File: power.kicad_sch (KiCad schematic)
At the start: 32 parts, among them Q3 AO3400A, U7 SIC431AED-T1-GE3, U9 TPS564247DRLR

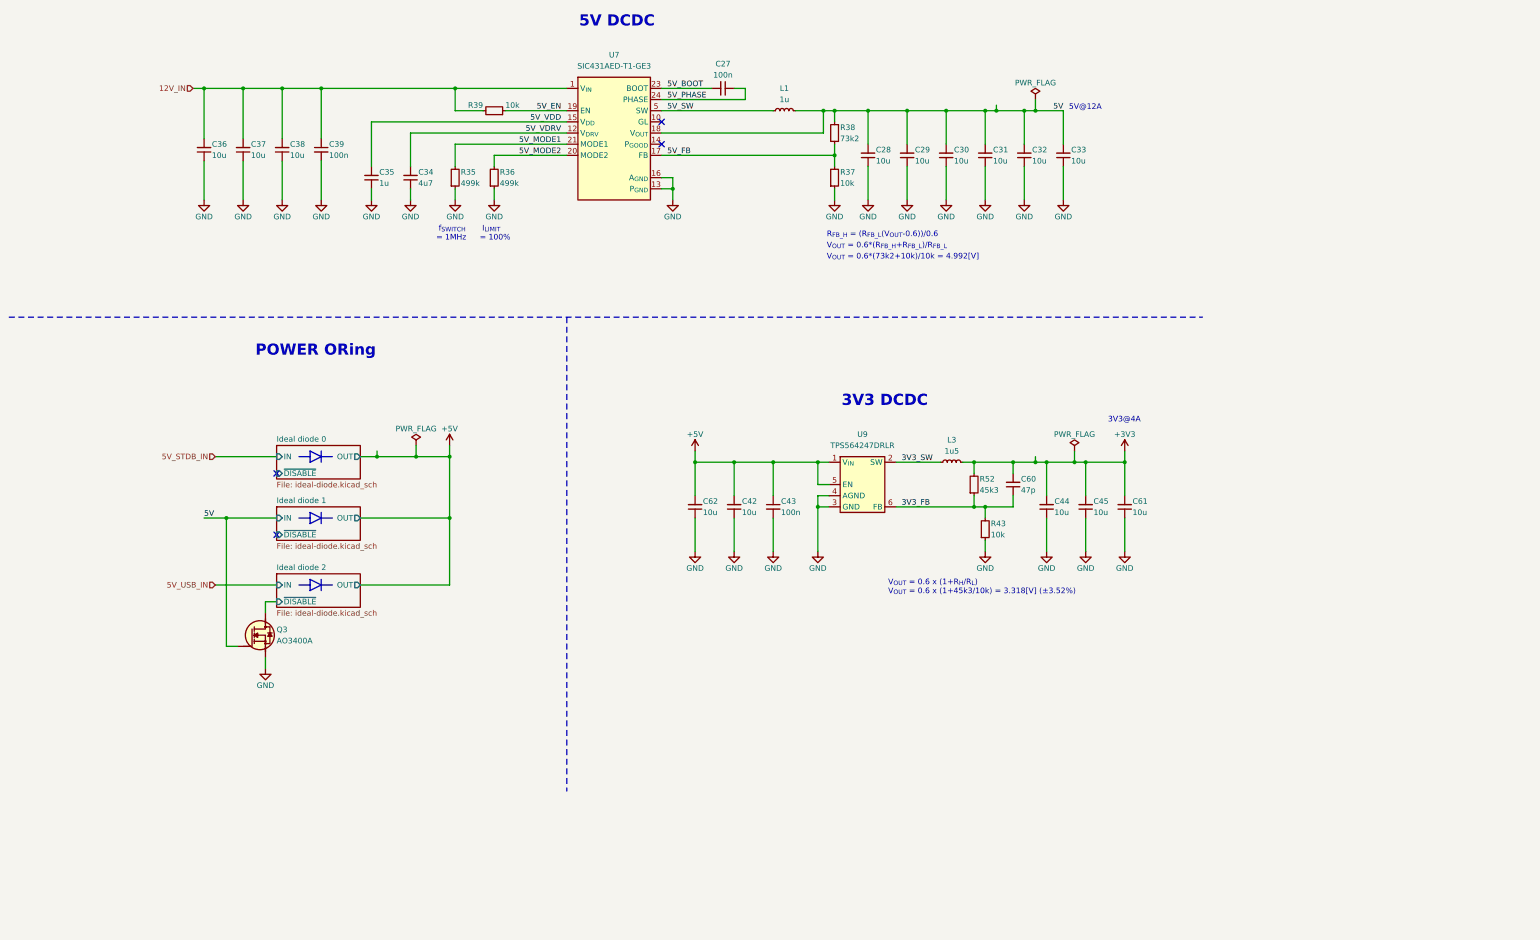
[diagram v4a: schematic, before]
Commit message: [#3] WIP: Clear ERC, re-annotate schematic
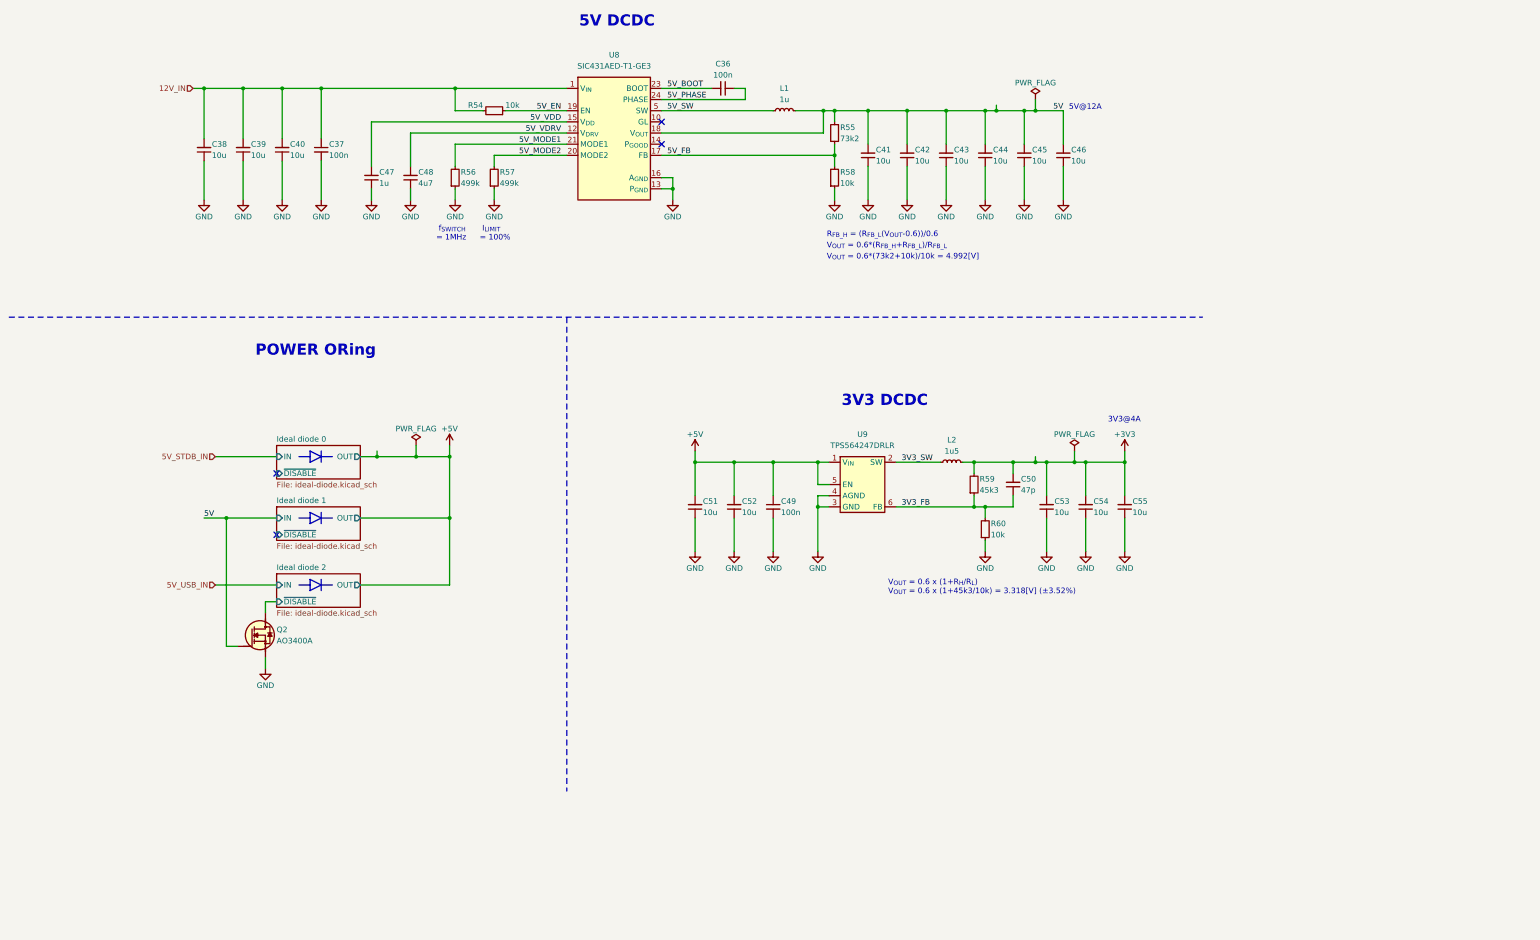
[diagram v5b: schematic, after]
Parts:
- renumbered C27 to C36, C39 to C37, C36 to C38, C37 to C39, C38 to C40, C28 to C41, C29 to C42, C30 to C43, C31 to C44, C32 to C45, C33 to C46, C35 to C47, C34 to C48, C43 to C49, C60 to C50, C62 to C51, C42 to C52, C44 to C53, C45 to C54, C61 to C55, L3 to L2, Q3 to Q2, R39 to R54, R38 to R55, R35 to R56, R36 to R57, R37 to R58, R52 to R59, R43 to R60, U7 to U8

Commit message: [#3] Add 0R to DC-DC outputs, add 5V->3V3 power sequencing
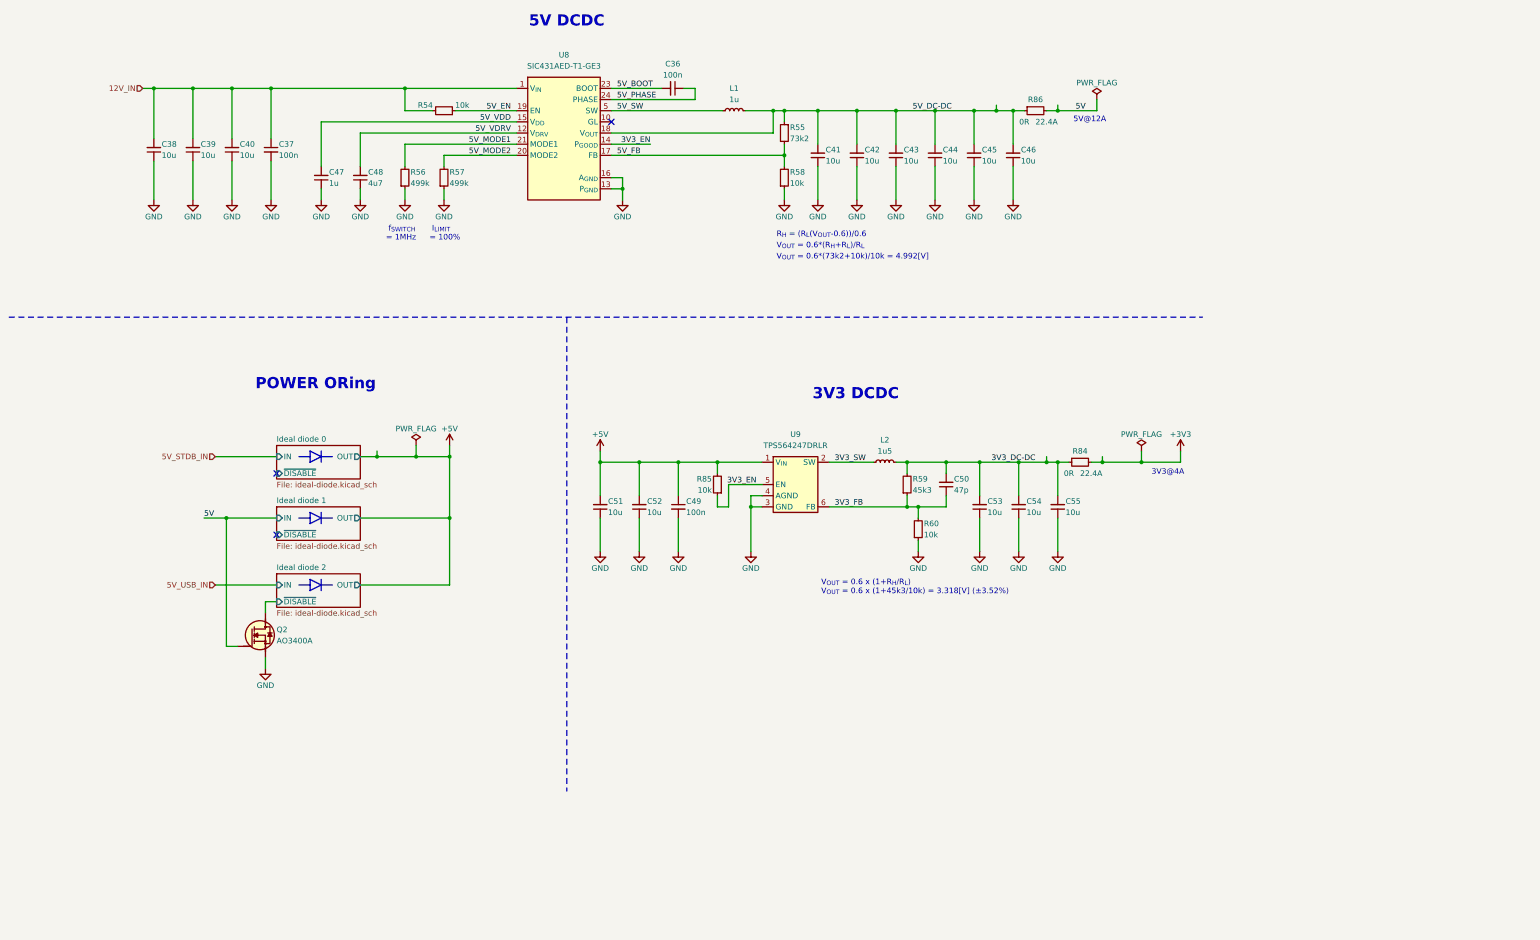
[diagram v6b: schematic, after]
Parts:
- added R84, R86: R-0R-22.4A-0603, DW-footprints:R_0603_1608Metric, symbol DW-resistors:R-0R-22.4A-0603
- added R85: R-10k-0402, DW-footprints:R_0402_1005Metric, symbol DW-resistors:R-10k-0402
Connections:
- net +3V3: now also R84.2; no longer C50.2, C53.2, C54.2, C55.2, L2.2, R59.2
- net +5V: now also R85.2; no longer U9.5 (EN)
- net 5V: now also R86.2; no longer C41.2, C42.2, C43.2, C44.2, C45.2, C46.2, L1.2, R55.1, U8.18 (V_{OUT})
- net 3V3_EN: now reaches U8.14 (P_{GOOD})
- net 3V3_EN: now also U9.5 (EN), R85.1
- new net 3V3_DC-DC: C50.2, C53.2, C54.2, C55.2, L2.2, R59.2, R84.1
- new net 5V_DC-DC: C41.2, C42.2, C43.2, C44.2, C45.2, C46.2, L1.2, R55.1, R86.1, U8.18 (V_{OUT})
- no-connect marks 4 -> 3
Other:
- note added: "R_{H} = (R_{L}(V_{OUT}-0.6))/0.6"
- note added: "V_{OUT} = 0.6*(R_{H}+R_{L})/R_{L}"
- note removed: "R_{FB_H} = (R_{FB_L}(V_{OUT}-0.6))/0.6"
- note removed: "V_{OUT} = 0.6*(R_{FB_H}+R_{FB_L})/R_{FB_L}"
- moved on the sheet: C36, C37, C38, C39, C40, C41, C42, C43, C44, C45, C46, C47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
